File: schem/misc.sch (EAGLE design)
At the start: 4 parts, among them IC1 74HC377N, IC2 74HC244N, IC3 74HC377N, IC4 74HC244N

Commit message: progress
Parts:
- added IC5, IC6, IC7, IC8, IC9: 74HC244N, 74xx-eu:74HC244N
- added R1, R2, R3, R4: (no value), rcl:R-US_0207/10
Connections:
- new net /BOE: IC8A.Y2, R3.2
- new net /BUSACK: IC9B.G
- new net /BUSREQ: R4.2
- new net /BWE: IC8A.Y1, R2.2
- new net /INT: R1.2
- new net /WE: IC8A.A1
- new net /WR: IC7A.G, IC7B.G
- new net ABH0: IC6A.A1
- new net ABH1: IC6A.A2
- new net ABH2: IC6A.A3
- new net ABH3: IC6A.A4
- new net ABH4: IC6B.A1
- new net ABH5: IC6B.A2
- new net ABH6: IC6B.A3
- new net ABH7: IC6B.A4
- new net ABL0: IC5A.A1
- new net ABL1: IC5A.A2
- new net ABL2: IC5A.A3
- new net ABL3: IC5A.A4
- new net ABL4: IC5B.A1
- new net ABL5: IC5B.A2
- new net ABL6: IC5B.A3
- new net ABL7: IC5B.A4
- new net AD0: IC5A.Y1
- new net AD1: IC5A.Y2
- new net AD10: IC6A.Y3
- new net AD11: IC6A.Y4
- new net AD12: IC6B.Y1
- new net AD13: IC6B.Y2
- new net AD14: IC6B.Y3
- new net AD15: IC6B.Y4
- new net AD2: IC5A.Y3
- new net AD3: IC5A.Y4
- new net AD4: IC5B.Y1
- new net AD5: IC5B.Y2
- new net AD6: IC5B.Y3
- new net AD7: IC5B.Y4
- new net AD8: IC6A.Y1
- new net AD9: IC6A.Y2
- new net BUSACK: IC5A.G, IC5B.G, IC6A.G, IC6B.G, IC8A.G, IC9A.G
- new net DB0: IC7A.Y1
- new net DB1: IC7A.Y2
- new net DB2: IC7A.Y3
- new net DB3: IC7A.Y4
- new net DB4: IC7B.Y1
- new net DB5: IC7B.Y2
- new net DB6: IC7B.Y3
- new net DB7: IC7B.Y4
- new net IBF0: IC9B.A1
- new net IBF1: IC9B.A2
- new net IBF2: IC9B.A3
- new net IBF3: IC9B.A4
- new net IBR0: IC9A.A1
- new net IBR1: IC9A.A2
- new net IBR2: IC9A.A3
- new net IBR3: IC9A.A4
- new net IBS0: IC9A.Y1, IC9B.Y1
- new net IBS1: IC9A.Y2, IC9B.Y2
- new net IBS2: IC9A.Y3, IC9B.Y3
- new net IBS3: IC9A.Y4, IC9B.Y4
- new net VCC: R1.1, R2.1, R3.1, R4.1
- new net WR: IC8A.A2
- net IB0: now also IC7A.A1
- net IB1: now also IC7A.A2
- net IB2: now also IC7A.A3
- net IB3: now also IC7A.A4
- net IB4: now also IC7B.A1
- net IB5: now also IC7B.A2
- net IB6: now also IC7B.A3
- net IB7: now also IC7B.A4

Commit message: finished most schematics
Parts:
- added SV1, SV3, SV4, SV6, SV7: (no value), con-lstb:MA08-1
- added SV10, SV2, SV5, SV8, SV9: (no value), con-lstb:MA06-1
- added SV11, SV12, SV13: (no value), con-lstb:MA05-2
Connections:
- removed net /INT: R1.2
- new net /IRQ: R1.2, SV8.3, SV9.6
- new net GND: SV11.10, SV11.9, SV12.10, SV12.9, SV13.10, SV13.9, SV2.4, SV2.5, SV2.6, SV5.4, SV5.5, SV5.6, SV8.6
- new net RESET: SV10.1, SV8.4
- new net SYNC: SV10.2, SV8.5
- net /BOE: now also SV8.1
- net /BUSACK: now also SV9.2
- net /BUSREQ: now also SV9.3
- net /BWE: now also SV8.2
- net /WE: now also SV9.4
- net ABH0: now also SV12.1
- net ABH1: now also SV12.2
- net ABH2: now also SV12.3
- net ABH3: now also SV12.4
- net ABH4: now also SV12.5
- net ABH5: now also SV12.6
- net ABH6: now also SV12.7
- net ABH7: now also SV12.8
- net ABL0: now also SV11.1
- net ABL1: now also SV11.2
- net ABL2: now also SV11.3
- net ABL3: now also SV11.4
- net ABL4: now also SV11.5
- net ABL5: now also SV11.6
- net ABL6: now also SV11.7
- net ABL7: now also SV11.8
- net AD0: now also SV6.1
- net AD1: now also SV6.2
- net AD10: now also SV7.3
- net AD11: now also SV7.4
- net AD12: now also SV7.5
- net AD13: now also SV7.6
- net AD14: now also SV7.7
- net AD15: now also SV7.8
- net AD2: now also SV6.3
- net AD3: now also SV6.4
- net AD4: now also SV6.5
- net AD5: now also SV6.6
- net AD6: now also SV6.7
- net AD7: now also SV6.8
- net AD8: now also SV7.1
- net AD9: now also SV7.2
- net BUSACK: now also SV9.1
- net CLK: now also SV2.3
- net DB0: now also SV3.1
- net DB1: now also SV3.2
- net DB2: now also SV3.3
- net DB3: now also SV3.4
- net DB4: now also SV3.5
- net DB5: now also SV3.6
- net DB6: now also SV3.7
- net DB7: now also SV3.8
- net IB0: now also SV1.1
- net IB1: now also SV1.2
- net IB2: now also SV1.3
- net IB3: now also SV1.4
- net IB4: now also SV1.5
- net IB5: now also SV1.6
- net IB6: now also SV1.7
- net IB7: now also SV1.8
- net IBD2: now also SV13.1
- net IBD3: now also SV13.3
- net IBR0: now also SV10.3
- net IBR1: now also SV10.4
- net IBR2: now also SV10.5
- net IBR3: now also SV10.6
- net IBS0: now also SV13.2
- net IBS1: now also SV13.4
- net IBS2: now also SV13.6
- net IBS3: now also SV13.8
- net OB0: now also SV4.1
- net OB1: now also SV4.2
- net OB2: now also SV4.3
- net OB3: now also SV4.4
- net OB4: now also SV4.5
- net OB5: now also SV4.6
- net OB6: now also SV4.7
- net OB7: now also SV4.8
- net OBD2: now also SV13.5
- net OBD3: now also SV13.7
- net VCC: now also SV2.1, SV2.2, SV5.1, SV5.2, SV5.3
- net WR: now also SV9.5

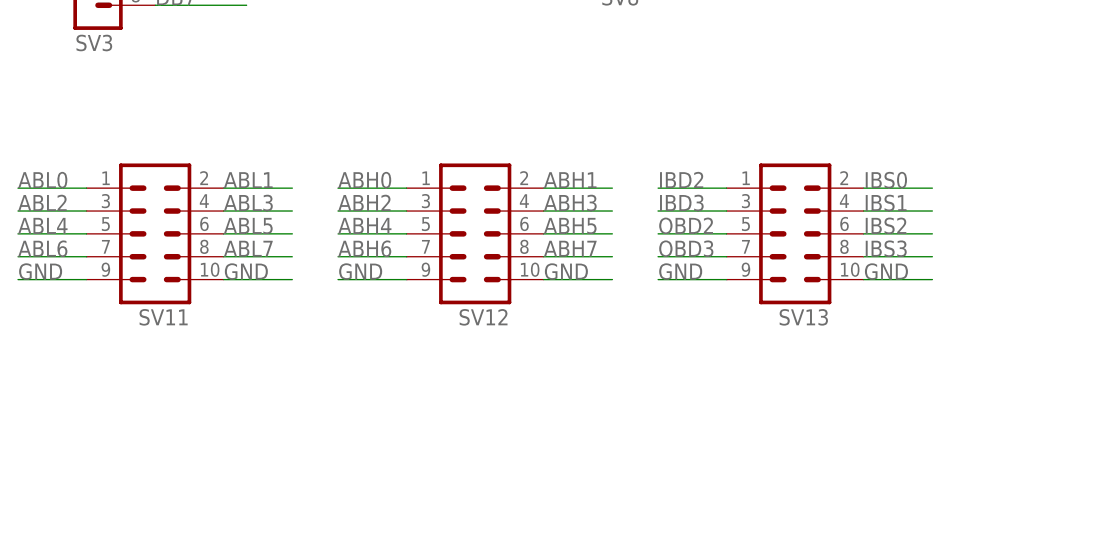
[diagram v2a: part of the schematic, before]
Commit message: adapted schematics for single headers
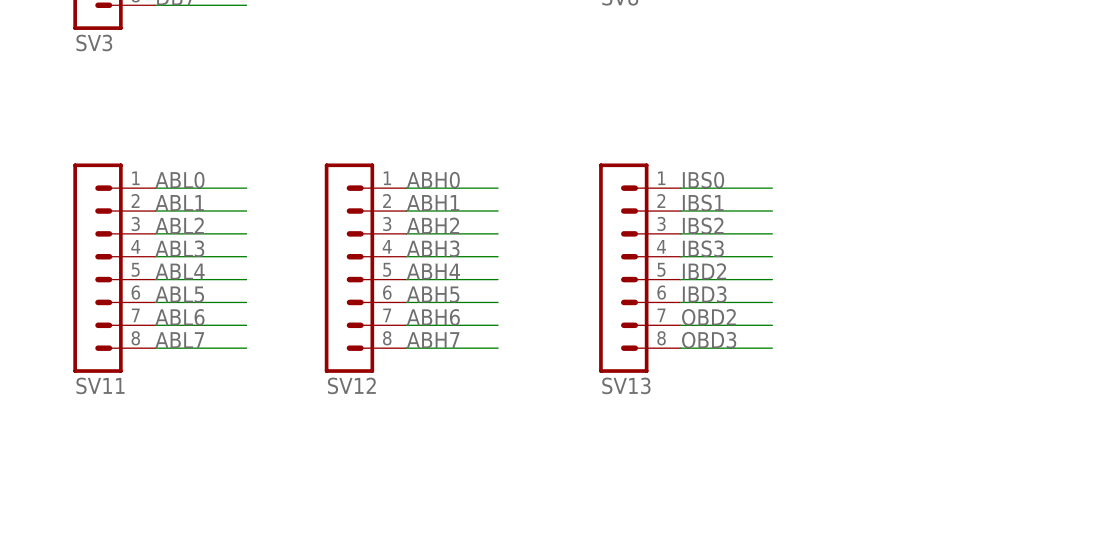
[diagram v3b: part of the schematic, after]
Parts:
- SV11, SV12, SV13: device con-lstb:MA05-2 -> con-lstb:MA08-1
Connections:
- net GND: no longer SV11.10, SV11.9, SV12.10, SV12.9, SV13.10, SV13.9
- net IBD2: now also SV13.5; no longer SV13.1
- net IBD3: now also SV13.6; no longer SV13.3
- net IBS0: now also SV13.1; no longer SV13.2
- net IBS1: now also SV13.2; no longer SV13.4
- net IBS2: now also SV13.3; no longer SV13.6
- net IBS3: now also SV13.4; no longer SV13.8
- net OBD2: now also SV13.7; no longer SV13.5
- net OBD3: now also SV13.8; no longer SV13.7
